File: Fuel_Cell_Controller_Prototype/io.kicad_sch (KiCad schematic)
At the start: 0 parts

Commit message: update
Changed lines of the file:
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@@
+    (stroke (width 0) (type default))
+  )
+  (wire (pts (xy 181.61 39.37) (xy 181.61 40.64))
     (stroke (width 0) (type default))
   )
@@
     (stroke (width 0) (type default))
   )
+  (wire (pts (xy 114.3 40.64) (xy 181.61 40.64))
+    (stroke (width 0) (type default))
+  )
+  (label "PA0" (at 114.3 40.64 0) (fields_autoplaced)
+    (effects (font (size 1.27 1.27)) (justify left bottom))
+  )
   (hierarchical_label "PD[0..15]" (shape bidirectional) (at 35.56 36.83 180) (fields_autoplaced)

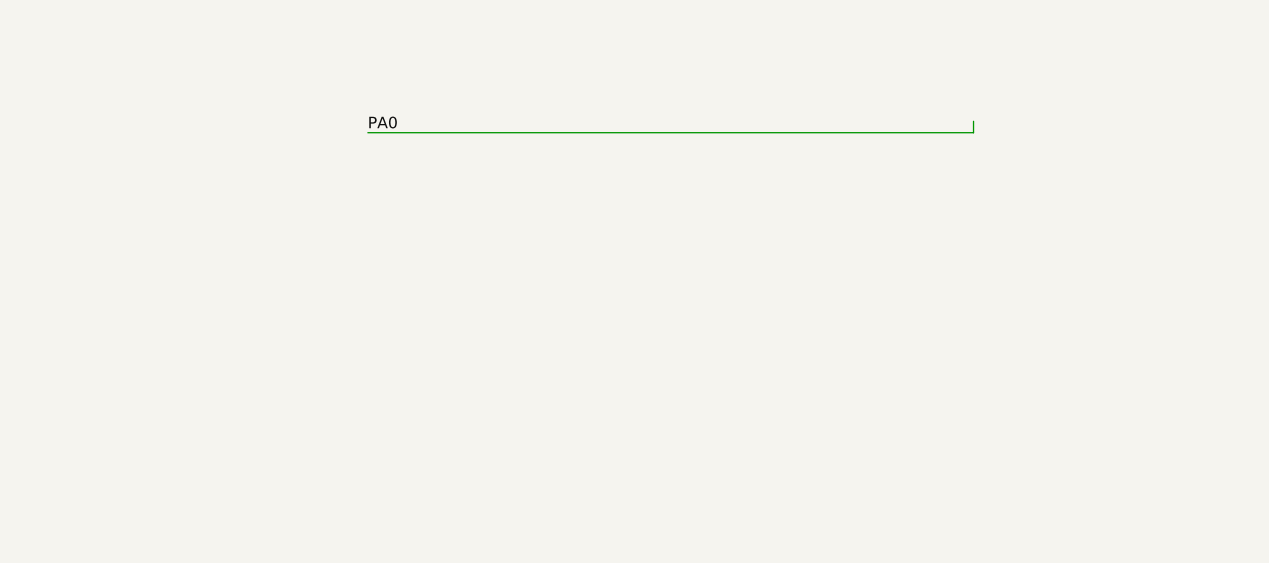
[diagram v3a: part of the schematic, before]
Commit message: Starting to add CAN infrastructure
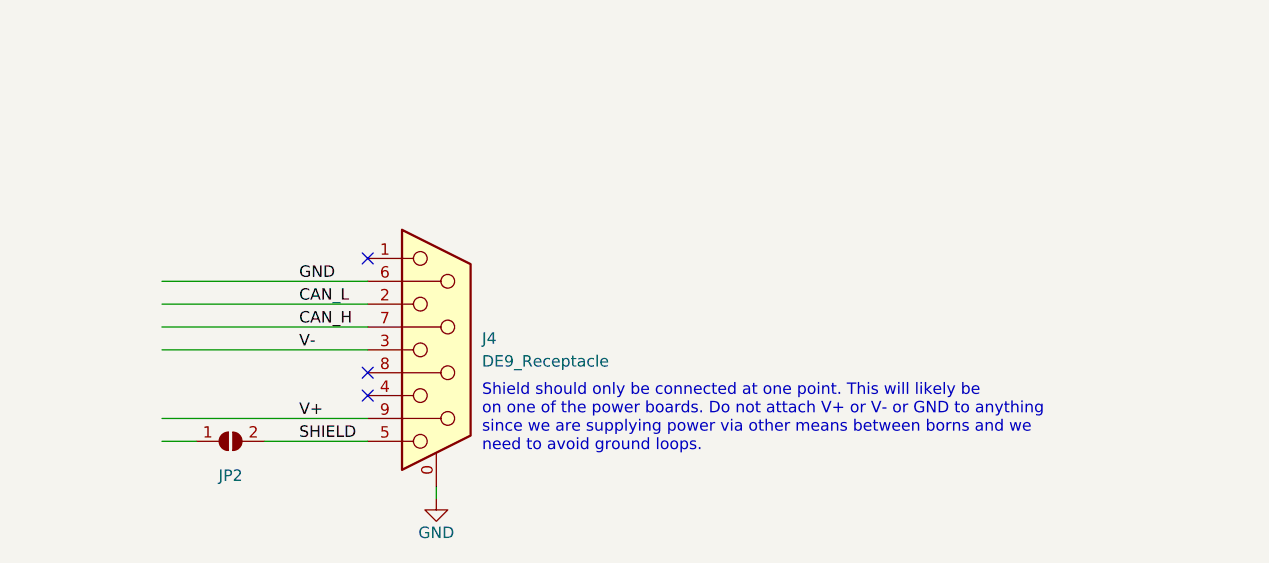
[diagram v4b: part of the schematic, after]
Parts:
- added J4: DE9_Receptacle, symbol Connector:DE9_Receptacle_MountingHoles
- added JP2: SolderJumper_2_Open, symbol Jumper:SolderJumper_2_Open
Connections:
- new net CAN_H: J4.7
- new net CAN_L: J4.2
- new net GND: J4.0 (PAD), J4.6
- new net SHIELD: J4.5, JP2.2 (B)
- new net V+: J4.9
- new net V-: J4.3
- no-connect marks 0 -> 3
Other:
- note added: "Shield should only be connected at one point. This will likely be on one of the power boards. Do not attach V+ or V- or GND to anything since we are supplying power via other means between borns and we need to avoid ground loops."
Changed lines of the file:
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@@
 (kicad_sch (version 20230121) (generator eeschema)
   (paper "A3")
+  (no_connect (at 114.3 54.61))
+  (no_connect (at 114.3 69.85))
+  (no_connect (at 114.3 67.31))
+  (wire (pts (xy 91.44 74.93) (xy 95.25 74.93))
+    (stroke (width 0) (type default))
+  )
+  (wire (pts (xy 102.87 74.93) (xy 114.3 74.93))
+    (stroke (width 0) (type default))
+  )
   (bus (pts (xy 35.56 41.91) (xy 59.69 41.91))
+    (stroke (width 0) (type default))
+  )
+  (wire (pts (xy 91.44 57.15) (xy 114.3 57.15))
     (stroke (width 0) (type default))
   )
@@
     (stroke (width 0) (type default))
   )
+  (wire (pts (xy 91.44 72.39) (xy 114.3 72.39))
+    (stroke (width 0) (type default))
+  )
   (bus (pts (xy 35.56 31.75) (xy 59.69 31.75))
     (stroke (width 0) (type default))
   )
-  (wire (pts (xy 181.61 39.37) (xy 181.61 40.64))
+  (wire (pts (xy 91.44 62.23) (xy 114.3 62.23))
     (stroke (width 0) (type default))
   )
@@
     (stroke (width 0) (type default))
   )
+  (wire (pts (xy 91.44 59.69) (xy 114.3 59.69))
+    (stroke (width 0) (type default))
+  )
   (bus (pts (xy 35.56 36.83) (xy 59.69 36.83))
+    (stroke (width 0) (type default))
+  )
+  (wire (pts (xy 91.44 64.77) (xy 114.3 64.77))
     (stroke (width 0) (type default))
   )
@@
     (stroke (width 0) (type default))
   )
-  (wire (pts (xy 114.3 40.64) (xy 181.61 40.64))
+  (wire (pts (xy 121.92 80.01) (xy 121.92 81.28))
     (stroke (width 0) (type default))
   )
-  (label "PA0" (at 114.3 40.64 0) (fields_autoplaced)
+  (text "Shield should only be connected at one point. This will likely be\non one of the power boards. Do not attach V+ or V- or GND to anything\nsince we are supplying power via other means between borns and we \nneed to avoid ground loops."
+    (at 127 76.2 0)
+    (effects (font (size 1.27 1.27)) (justify left bottom))
+  )
+  (label "CAN_H" (at 106.68 62.23 0) (fields_autoplaced)
+    (effects (font (size 1.27 1.27)) (justify left bottom))
+  )
+  (label "V+" (at 106.68 72.39 0) (fields_autoplaced)
+    (effects (font (size 1.27 1.27)) (justify left bottom))
+  )
+  (label "V-" (at 106.68 64.77 0) (fields_autoplaced)
+    (effects (font (size 1.27 1.27)) (justify left bottom))
+  )
+  (label "CAN_L" (at 106.68 59.69 0) (fields_autoplaced)
+    (effects (font (size 1.27 1.27)) (justify left bottom))
+  )
+  (label "GND" (at 106.68 57.15 0) (fields_autoplaced)
+    (effects (font (size 1.27 1.27)) (justify left bottom))
+  )
+  (label "SHIELD" (at 106.68 74.93 0) (fields_autoplaced)
     (effects (font (size 1.27 1.27)) (justify left bottom))
   )
@@
     (effects (font (size 1.27 1.27)) (justify right))
   )
+  (symbol (lib_id "Jumper:SolderJumper_2_Open") (at 99.06 74.93 0) (unit 1)
+    (in_bom yes) (on_board yes) (dnp no)
+    (property "Reference" "JP2" (at 99.06 78.74 0)
+      (effects (font (size 1.27 1.27)))
+    )
+    (property "Value" "SolderJumper_2_Open" (at 99.06 80.01 0)
+      (effects (font (size 1.27 1.27)) hide)
+    )
+    (property "Footprint" "" (at 99.06 74.93 0)
+      (effects (font (size 1.27 1.27)) hide)
+    )
+    (property "Datasheet" "~" (at 99.06 74.93 0)
+      (effects (font (size 1.27 1.27)) hide)
+    )
+    (pin "1")
+    (pin "2")
+    (instances
+      (project "Fuel_Cell_Controller_Prototype"
+        (path "/f651cec9-411c-4a4e-a163-5c49adbe6a12/593c7e68-7c5e-4ef7-bd05-a128c02972b0"
+          (reference "JP2") (unit 1)
+        )
+      )
+    )
+  )
+  (symbol (lib_id "power:GND") (at 121.92 81.28 0) (unit 1)
+    (in_bom yes) (on_board yes) (dnp no)
+    (property "Reference" "#PWR031" (at 121.92 87.63 0)
+      (effects (font (size 1.27 1.27)) hide)
+    )
+    (property "Value" "GND" (at 121.92 85.09 0)
+      (effects (font (size 1.27 1.27)))
+    )
+    (property "Footprint" "" (at 121.92 81.28 0)
+      (effects (font (size 1.27 1.27)) hide)
+    )
+    (property "Datasheet" "" (at 121.92 81.28 0)
+      (effects (font (size 1.27 1.27)) hide)
+    )
+    (pin "1")
+    (instances
+      (project "Fuel_Cell_Controller_Prototype"
+        (path "/f651cec9-411c-4a4e-a163-5c49adbe6a12/593c7e68-7c5e-4ef7-bd05-a128c02972b0"
+          (reference "#PWR031") (unit 1)
+        )
+      )
+    )
+  )
+  (symbol (lib_id "Connector:DE9_Receptacle_MountingHoles") (at 121.92 64.77 0) (unit 1)
+    (in_bom yes) (on_board yes) (dnp no) (fields_autoplaced)
+    (property "Reference" "J4" (at 127 63.5 0)
+      (effects (font (size 1.27 1.27)) (justify left))
+    )
+    (property "Value" "DE9_Receptacle" (at 127 66.04 0)
+      (effects (font (size 1.27 1.27)) (justify left))
+    )
+    (property "Footprint" "" (at 121.92 64.77 0)
+      (effects (font (size 1.27 1.27)) hide)
+    )
+    (property "Datasheet" " ~" (at 121.92 64.77 0)
+      (effects (font (size 1.27 1.27)) hide)
+    )
+    (pin "0")
+    (pin "1")
+    (pin "2")
+    (pin "3")
+    (pin "4")
+    (pin "5")
+    (pin "6")
+    (pin "7")
+    (pin "8")
+    (pin "9")
+    (instances
+      (project "Fuel_Cell_Controller_Prototype"
+        (path "/f651cec9-411c-4a4e-a163-5c49adbe6a12/593c7e68-7c5e-4ef7-bd05-a128c02972b0"
+          (reference "J4") (unit 1)
+        )
+      )
+    )
+  )
 )

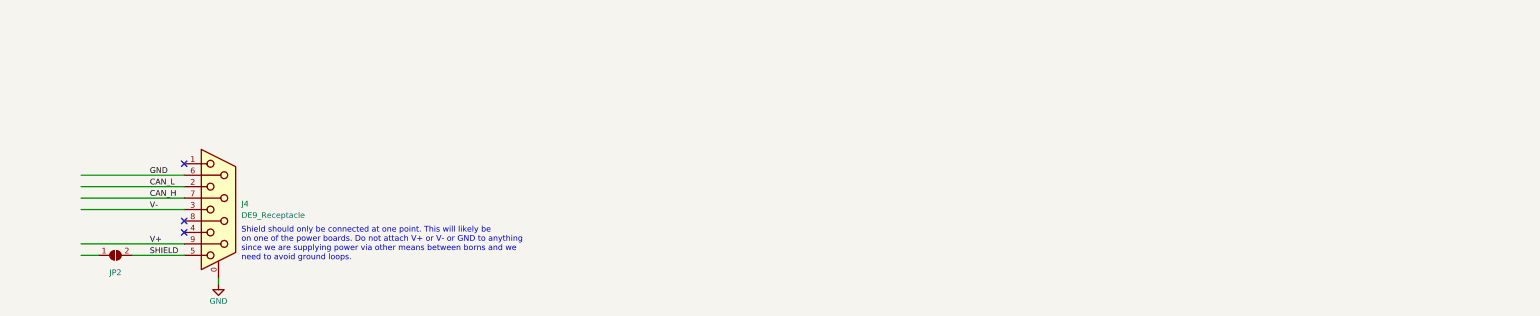
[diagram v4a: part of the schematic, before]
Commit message: Added some more CAN supporting hardware
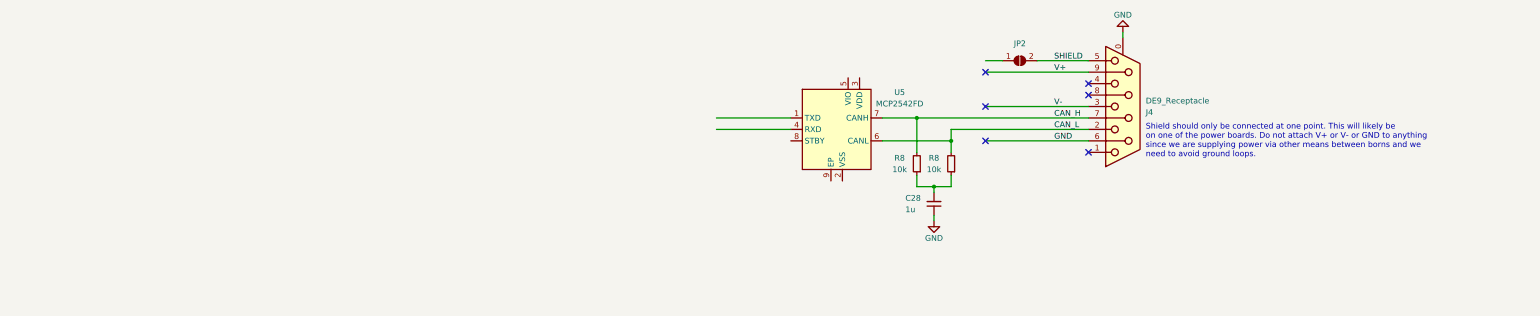
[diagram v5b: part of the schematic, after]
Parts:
- added C28: 1u, symbol Device:C_Small
- added R8 (x2): 10k, symbol Device:R_Small
- added U5: MCP2542FD, Package_DFN_QFN:DFN-8-1EP_3x3mm_P0.65mm_EP1.55x2.4mm, symbol FCC_Parts:MCP2542FD
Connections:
- net CAN_H: now also R8.2, U5.7 (CANH)
- net CAN_L: now also R8.2, U5.6 (CANL)
- net GND: now also C28.1
- new net: C28.2, R8.1, R8.1
- no-connect marks 3 -> 6
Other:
- moved on the sheet: J4, JP2

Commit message: Revert "huh"
This reverts commit 7bb3ffd8f300d735453e7bd9492734dd47e7a050.
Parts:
- added C28: 0u1, symbol Device:C_Small
- added D13, D14: D, symbol Device:D
- added J6: DA15_Receptacle_MountingHoles, symbol Connector:DA15_Receptacle_MountingHoles
- added JP4, JP6: SolderJumper_2_Open, symbol Jumper:SolderJumper_2_Open
- added Q1 (x2): NMOS, symbol Simulation_SPICE:NMOS
- added R8 (x2): 220, symbol Device:R_Small
- added R8 (x2): 100k, symbol Device:R_Small
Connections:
- net CAN_H: now also JP4.1 (A); no longer R8.2
- net CAN_L: now also JP6.1 (A); no longer R8.2
- net GND: now also JP2.1 (A), U5.2 (VSS), U5.9 (EP), C28.1, J6.0 (PAD), J6.15 (P15), J6.8
- net CAN2_RX: now reaches U5.1 (TXD)
- net +5V: now reaches U5.3 (VDD)
- net +5V: now also C28.2
- net CAN2_TX: now reaches U5.4 (RXD)
- net VDDA: now reaches U5.5 (VIO)
- new net: JP4.2 (B), R8.2
- new net: Q1.2 (G), R8.1, R8.1 (x2)
- new net: JP6.2 (B), R8.2
- new net GNDPWR: Q1.3 (S), Q1.3 (S), R8.2, R8.2
- new net PF1: R8.2
- new net PF2: R8.2
- new net PURGE_RETURN: D14.2 (A), J6.10 (P10), Q1.1 (D)
- new net SUPPLY_RETURN: D13.2 (A), J6.2, Q1.1 (D)
- new net UNPROTECTED_12V: D13.1 (K), D14.1 (K), J6.1, J6.9 (P9)
- no-connect marks 6 -> 7
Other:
- note added: "CANBus Transciever and Receptacle"
- note added: "Receptacle to Fuel Cell"
- note added: "Should we add optocouplers? Select SMD diodes with high reverse volt prolly 50V High current tolerant NMOS as well. Check solenoid current req"
- note added: "Solenoid Valve Controls"
- moved on the sheet: C28, J4, JP2, R8, U5

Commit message: huh
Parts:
- removed C28: 0u1, symbol Device:C_Small
- removed D13, D14: D, symbol Device:D
- removed J6: DA15_Receptacle_MountingHoles, symbol Connector:DA15_Receptacle_MountingHoles
- removed JP4, JP6: SolderJumper_2_Open, symbol Jumper:SolderJumper_2_Open
- removed Q1 (x2): NMOS, symbol Simulation_SPICE:NMOS
- removed R8 (x2): 220, symbol Device:R_Small
- removed R8 (x2): 100k, symbol Device:R_Small
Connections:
- net CAN_H: now also R8.2
- net CAN_L: now also R8.2
- net GND: no longer JP2.1 (A), U5.2 (VSS), U5.9 (EP)
- net +5V: no longer names the net of U5.3 (VDD)
- net CAN2_RX: no longer names the net of U5.1 (TXD)
- net CAN2_TX: no longer names the net of U5.4 (RXD)
- net VDDA: no longer names the net of U5.5 (VIO)
- no-connect marks 7 -> 6
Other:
- note removed: "CANBus Transciever and Receptacle"
- note removed: "Receptacle to Fuel Cell"
- note removed: "Should we add optocouplers? Select SMD diodes with high reverse volt prolly 50V High current tolerant NMOS as well. Check solenoid current req"
- note removed: "Solenoid Valve Controls"
- moved on the sheet: C28, J4, JP2, R8, U5
